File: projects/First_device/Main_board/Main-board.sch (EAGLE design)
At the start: 52 parts, among them Q1 BC847ALT1SMD, Q2 BC847ALT1SMD, Q3 BC847ALT1SMD, Q4 BC847ALT1SMD, T1 BCR108E6327, T2 BCR108E6327, T3 BCR108E6327, T4 BCR108E6327, X1 2EHDCR-5.08-10P, X2 2EHDCR-5.08-08P

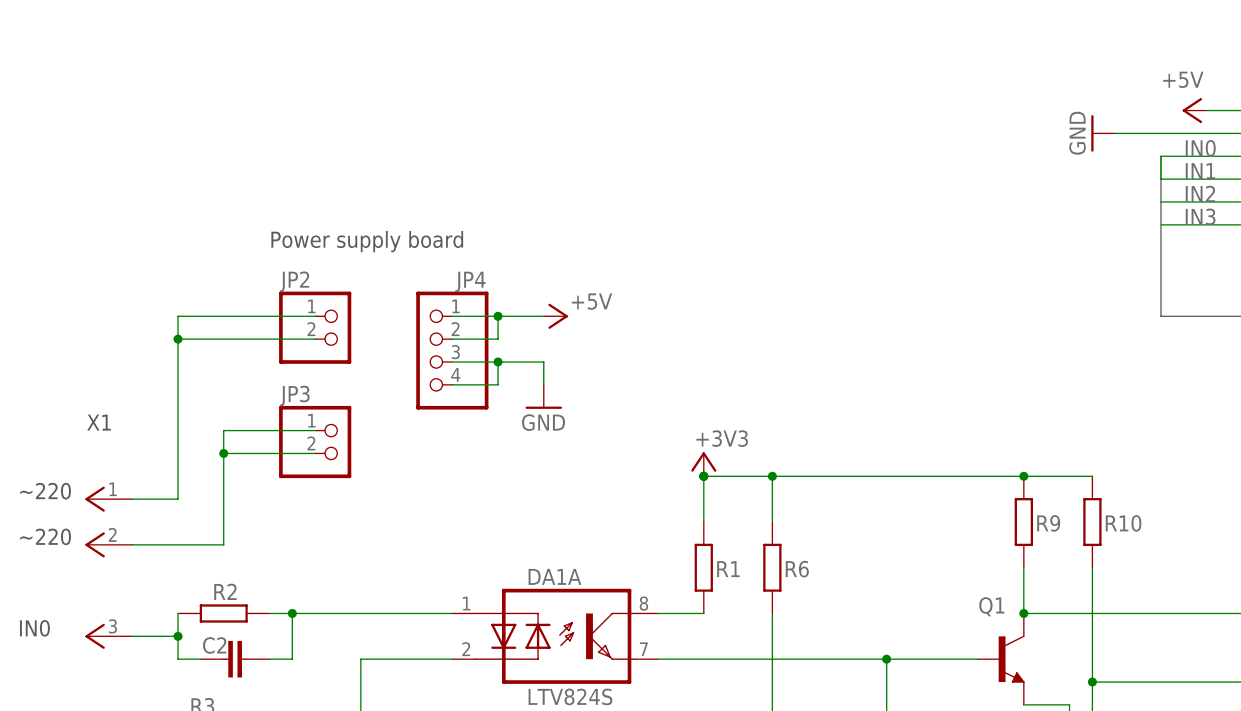
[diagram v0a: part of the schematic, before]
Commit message: AC/DC converter is added
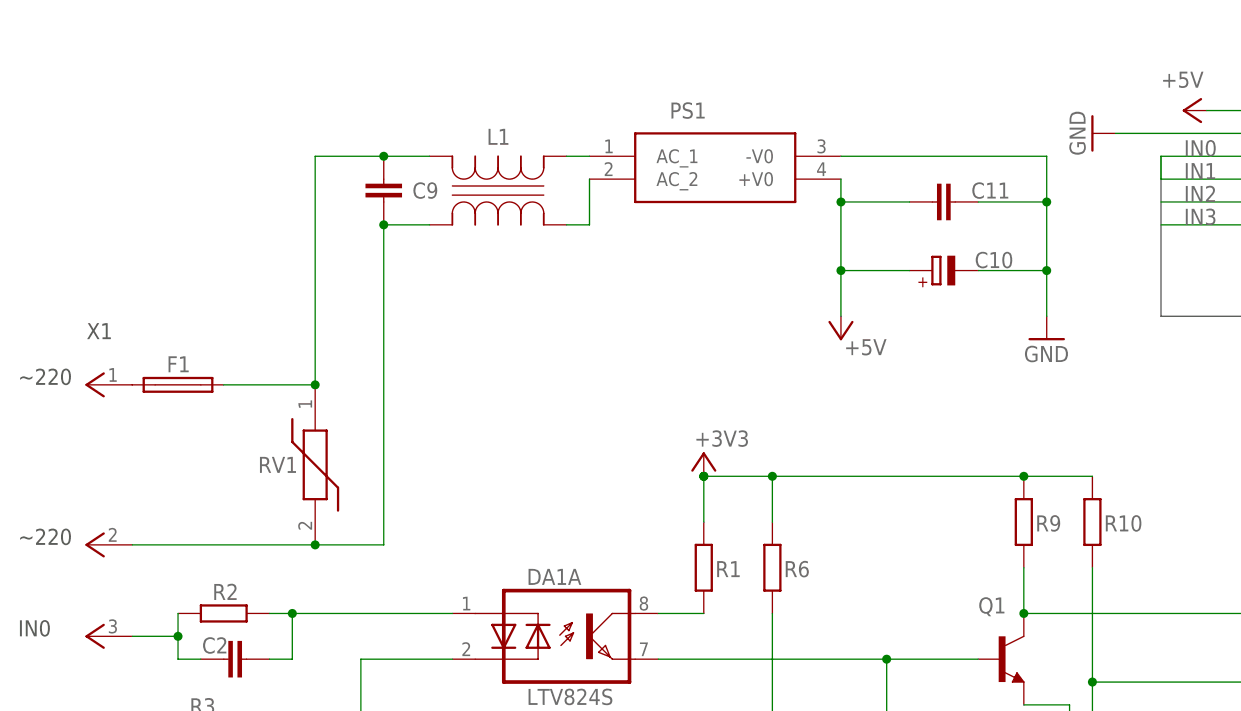
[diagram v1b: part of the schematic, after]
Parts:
- removed JP2, JP3: NOT INSTALLED, pinhead:PINHD-1X2
- removed JP4: NOT INSTALLED, pinhead:PINHD-1X4
- added C10: 220uF, rcl:CPOL-EUD/7343-31W
- added C11: 0,1u, rcl:C-EUC0603
- added C9: R46KI310000M1K, My_lib:R46KI310000M1K
- added F1: 0,5A, fuse:TR5
- added L1: DLW5BSN152SQ2L, My_lib:DLW5BSN152SQ2L
- added PS1: HLK-10M05, My_lib:HLK-10M05
- added RV1: VDR-10D561KJ, My_lib:VDR-10D561KJ
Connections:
- new net N$12: C9.2, F1.1, L1.1, RV1.1
- new net N$13: L1.2, PS1.AC_1
- new net N$26: C9.1, L1.4, RV1.2, X1G$2.1
- net +5V: now also C10.+, C11.1, PS1.+V0; no longer JP4.1, JP4.2
- net GND: now also C10.-, C11.2, PS1.-V0; no longer JP4.3, JP4.4
- net N$15: now also L1.3, PS1.AC_2; no longer JP3.1, JP3.2, X1G$2.1
- net N$16: now also F1.2; no longer JP2.1, JP2.2
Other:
- note removed: "Power supply board"

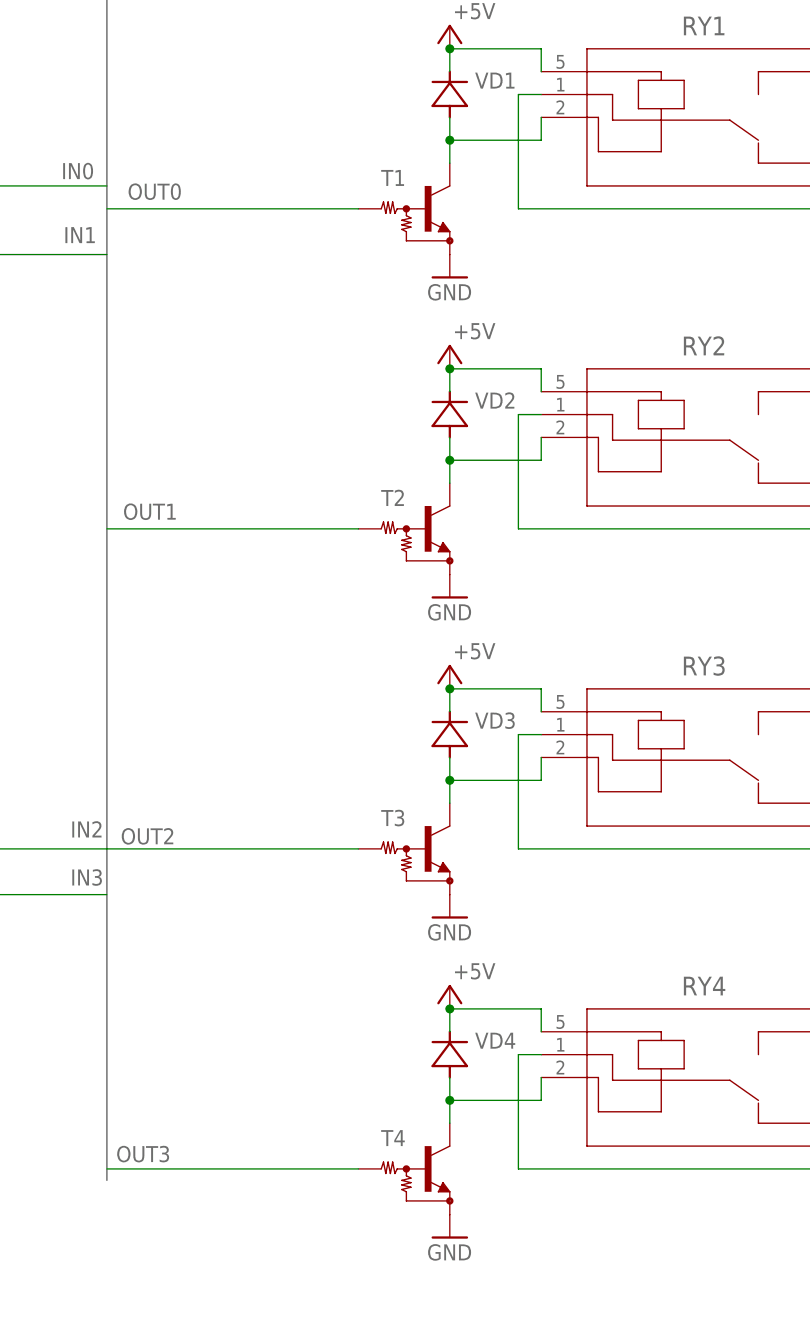
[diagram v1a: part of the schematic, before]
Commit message: Update BCR108 on main board
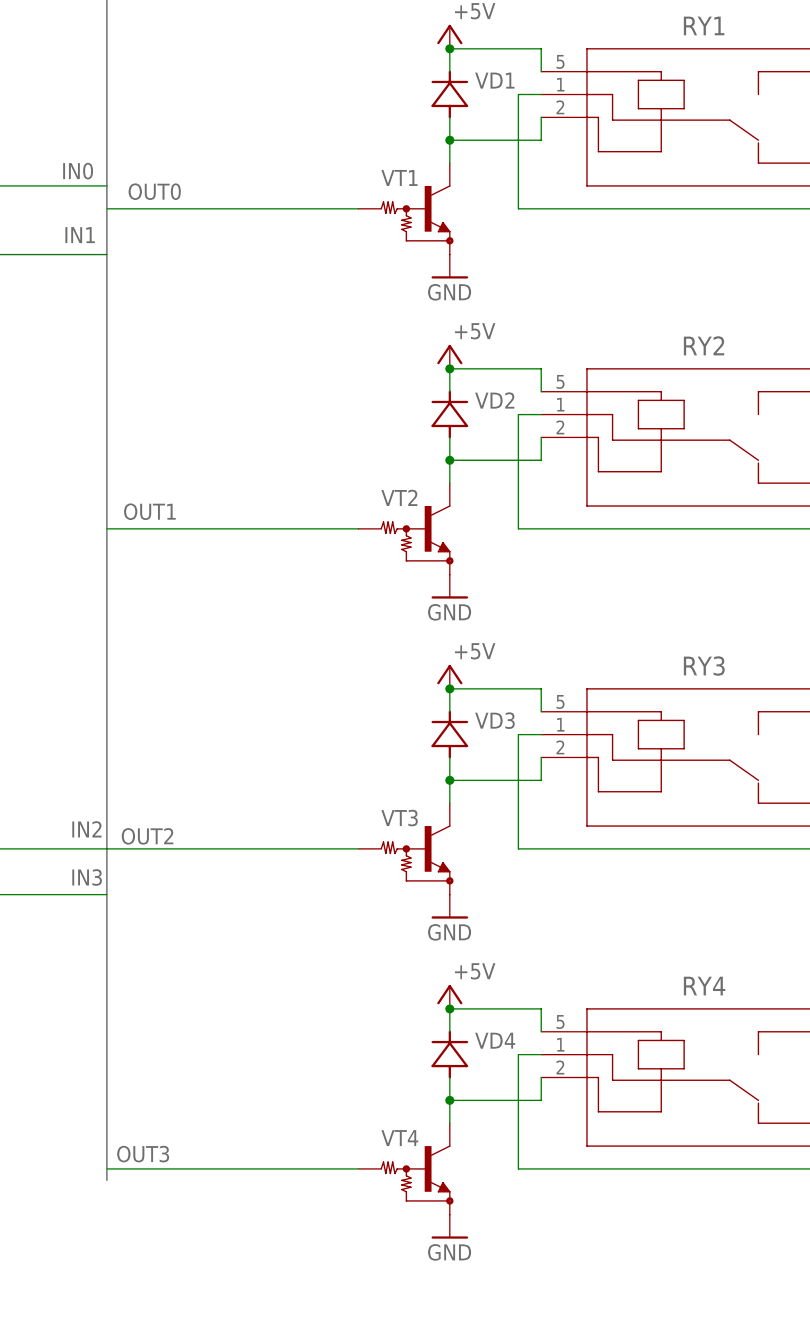
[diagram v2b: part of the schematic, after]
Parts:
- removed T1, T2, T3, T4: BCR108E6327, My_lib:BCR108BCR108E6327SC59-BEC
- added VT1, VT2, VT3, VT4: BCR108E6327, My_lib:BCR108E6327
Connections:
- net GND: now also VT1.2, VT2.2, VT3.2, VT4.2; no longer T1.E, T2.E, T3.E, T4.E
- net N$33: now also VT2.3; no longer T2.C
- net N$34: now also VT1.3; no longer T1.C
- net N$35: now also VT3.3; no longer T3.C
- net N$36: now also VT4.3; no longer T4.C
- net OUT0: now also VT1.1; no longer T1.B
- net OUT1: now also VT2.1; no longer T2.B
- net OUT2: now also VT3.1; no longer T3.B
- net OUT3: now also VT4.1; no longer T4.B
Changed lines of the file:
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@@
 </part>
 <part name="VD1" library="My_lib" deviceset="LL4148" device="" package3d_urn="urn:adsk.eagle:package:43405/2"/>
-<part name="T1" library="My_lib" deviceset="BCR108" device="SC59-BEC" package3d_urn="urn:adsk.eagle:package:28754/2" technology="BCR108E6327" value="BCR108E6327 "/>
 <part name="X1" library="My_lib" deviceset="2EHDCR-5.08-10P" device=""/>
 <part name="X2" library="My_lib" deviceset="2EHDCR-5.08-08P" device=""/>
@@
 <part name="P+1" library="supply1" library_urn="urn:adsk.eagle:library:371" deviceset="+5V" device=""/>
 <part name="VD2" library="My_lib" deviceset="LL4148" device="" package3d_urn="urn:adsk.eagle:package:43405/2"/>
-<part name="T2" library="My_lib" deviceset="BCR108" device="SC59-BEC" package3d_urn="urn:adsk.eagle:package:28754/2" technology="BCR108E6327" value="BCR108E6327 "/>
 <part name="GND4" library="supply1" library_urn="urn:adsk.eagle:library:371" deviceset="GND" device=""/>
 <part name="P+2" library="supply1" library_urn="urn:adsk.eagle:library:371" deviceset="+5V" device=""/>
 <part name="VD3" library="My_lib" deviceset="LL4148" device="" package3d_urn="urn:adsk.eagle:package:43405/2"/>
-<part name="T3" library="My_lib" deviceset="BCR108" device="SC59-BEC" package3d_urn="urn:adsk.eagle:package:28754/2" technology="BCR108E6327" value="BCR108E6327 "/>
 <part name="GND5" library="supply1" library_urn="urn:adsk.eagle:library:371" deviceset="GND" device=""/>
 <part name="P+3" library="supply1" library_urn="urn:adsk.eagle:library:371" deviceset="+5V" device=""/>
 <part name="VD4" library="My_lib" deviceset="LL4148" device="" package3d_urn="urn:adsk.eagle:package:43405/2"/>
-<part name="T4" library="My_lib" deviceset="BCR108" device="SC59-BEC" package3d_urn="urn:adsk.eagle:package:28754/2" technology="BCR108E6327" value="BCR108E6327 "/>
 <part name="GND6" library="supply1" library_urn="urn:adsk.eagle:library:371" deviceset="GND" device=""/>
 <part name="P+4" library="supply1" library_urn="urn:adsk.eagle:library:371" deviceset="+5V" device=""/>
@@
 <attribute name="VOLTAGE" value="50V"/>
 </part>
+<part name="VT1" library="My_lib" deviceset="BCR108" device="E6327"/>
+<part name="VT2" library="My_lib" deviceset="BCR108" device="E6327"/>
+<part name="VT3" library="My_lib" deviceset="BCR108" device="E6327"/>
+<part name="VT4" library="My_lib" deviceset="BCR108" device="E6327"/>
 </parts>
 <sheets>
@@
 <attribute name="NAME" x="129.3114" y="98.9584" size="1.778" layer="95" rot="R180"/>
 </instance>
-<instance part="T1" gate="G$1" x="119.38" y="83.82" smashed="yes">
-<attribute name="NAME" x="114.3" y="86.36" size="1.778" layer="95"/>
-<attribute name="VALUE" x="109.22" y="88.9" size="1.778" layer="96" display="off"/>
-</instance>
 <instance part="X1" gate="G$1" x="-53.34" y="106.68" smashed="yes"/>
 <instance part="X1" gate="G$2" x="-53.34" y="88.9" smashed="yes"/>
@@
 <attribute name="NAME" x="129.3114" y="63.3984" size="1.778" layer="95" rot="R180"/>
 </instance>
-<instance part="T2" gate="G$1" x="119.38" y="48.26" smashed="yes">
-<attribute name="NAME" x="114.3" y="50.8" size="1.778" layer="95"/>
-<attribute name="VALUE" x="109.22" y="53.34" size="1.778" layer="96" display="off"/>
-</instance>
 <instance part="GND4" gate="1" x="121.92" y="40.64" smashed="yes">
 <attribute name="VALUE" x="119.38" y="38.1" size="1.778" layer="96"/>
@@
 <attribute name="NAME" x="129.3114" y="27.8384" size="1.778" layer="95" rot="R180"/>
 </instance>
-<instance part="T3" gate="G$1" x="119.38" y="12.7" smashed="yes">
-<attribute name="NAME" x="114.3" y="15.24" size="1.778" layer="95"/>
-<attribute name="VALUE" x="109.22" y="17.78" size="1.778" layer="96" display="off"/>
-</instance>
 <instance part="GND5" gate="1" x="121.92" y="5.08" smashed="yes">
 <attribute name="VALUE" x="119.38" y="2.54" size="1.778" layer="96"/>
@@
 <instance part="VD4" gate="G$1" x="121.92" y="-10.16" smashed="yes" rot="R90">
 <attribute name="NAME" x="129.3114" y="-7.7216" size="1.778" layer="95" rot="R180"/>
-</instance>
-<instance part="T4" gate="G$1" x="119.38" y="-22.86" smashed="yes">
-<attribute name="NAME" x="114.3" y="-20.32" size="1.778" layer="95"/>
-<attribute name="VALUE" x="109.22" y="-17.78" size="1.778" layer="96" display="off"/>
 </instance>
 <instance part="GND6" gate="1" x="121.92" y="-30.48" smashed="yes">
@@
 <attribute name="STYPE" x="38.1" y="132.08" size="1.778" layer="96" rot="R90" display="off"/>
 <attribute name="VOLTAGE" x="38.1" y="132.08" size="1.778" layer="96" rot="R90" display="off"/>
+</instance>
+<instance part="VT1" gate="G$1" x="119.38" y="83.82" smashed="yes">
+<attribute name="NAME" x="114.3" y="86.36" size="1.778" layer="95"/>
+<attribute name="VALUE" x="109.22" y="88.9" size="1.778" layer="96" display="off"/>
+</instance>
+<instance part="VT2" gate="G$1" x="119.38" y="48.26" smashed="yes">
+<attribute name="NAME" x="114.3" y="50.8" size="1.778" layer="95"/>
+<attribute name="VALUE" x="109.22" y="53.34" size="1.778" layer="96" display="off"/>
+</instance>
+<instance part="VT3" gate="G$1" x="119.38" y="12.7" smashed="yes">
+<attribute name="NAME" x="114.3" y="15.24" size="1.778" layer="95"/>
+<attribute name="VALUE" x="109.22" y="17.78" size="1.778" layer="96" display="off"/>
+</instance>
+<instance part="VT4" gate="G$1" x="119.38" y="-22.86" smashed="yes">
+<attribute name="NAME" x="114.3" y="-20.32" size="1.778" layer="95"/>
+<attribute name="VALUE" x="109.22" y="-17.78" size="1.778" layer="96" display="off"/>
 </instance>
 </instances>
@@
 </segment>
 <segment>
-<pinref part="GND3" gate="1" pin="GND"/>
-<pinref part="T1" gate="G$1" pin="E"/>
-</segment>
-<segment>
-<pinref part="GND4" gate="1" pin="GND"/>
-<pinref part="T2" gate="G$1" pin="E"/>
-</segment>
-<segment>
-<pinref part="GND5" gate="1" pin="GND"/>
-<pinref part="T3" gate="G$1" pin="E"/>
-</segment>
-<segment>
-<pinref part="GND6" gate="1" pin="GND"/>
-<pinref part="T4" gate="G$1" pin="E"/>
-</segment>
-<segment>
 <pinref part="GND7" gate="1" pin="GND"/>
 <wire x1="58.42" y1="139.7" x2="78.74" y2="139.7" width="0.1524" layer="91"/>
@@
 <wire x1="43.18" y1="124.46" x2="50.8" y2="124.46" width="0.1524" layer="91"/>
 <junction x="50.8" y="124.46"/>
+</segment>
+<segment>
+<pinref part="GND3" gate="1" pin="GND"/>
+<pinref part="VT1" gate="G$1" pin="2"/>
+</segment>
+<segment>
+<pinref part="VT2" gate="G$1" pin="2"/>
+<pinref part="GND4" gate="1" pin="GND"/>
+</segment>
+<segment>
+<pinref part="VT3" gate="G$1" pin="2"/>
+<pinref part="GND5" gate="1" pin="GND"/>
+</segment>
+<segment>
+<pinref part="VT4" gate="G$1" pin="2"/>
+<pinref part="GND6" gate="1" pin="GND"/>
 </segment>
 </net>
@@
 <wire x1="121.92" y1="88.9" x2="121.92" y2="91.44" width="0.1524" layer="91"/>
 <junction x="121.92" y="91.44"/>
-<pinref part="T1" gate="G$1" pin="C"/>
+<pinref part="VT1" gate="G$1" pin="3"/>
 </segment>
 </net>
@@
 <wire x1="121.92" y1="53.34" x2="121.92" y2="55.88" width="0.1524" layer="91"/>
 <junction x="121.92" y="55.88"/>
-<pinref part="T2" gate="G$1" pin="C"/>
 <pinref part="RY2" gate="A" pin="2"/>
 <wire x1="132.08" y1="58.42" x2="132.08" y2="55.88" width="0.1524" layer="91"/>
+<pinref part="VT2" gate="G$1" pin="3"/>
 </segment>
 </net>
@@
 <wire x1="121.92" y1="17.78" x2="121.92" y2="20.32" width="0.1524" layer="91"/>
 <junction x="121.92" y="20.32"/>
-<pinref part="T3" gate="G$1" pin="C"/>
 <pinref part="RY3" gate="A" pin="2"/>
 <wire x1="132.08" y1="22.86" x2="132.08" y2="20.32" width="0.1524" layer="91"/>
+<pinref part="VT3" gate="G$1" pin="3"/>
 </segment>
 </net>
@@
 <wire x1="121.92" y1="-17.78" x2="121.92" y2="-15.24" width="0.1524" layer="91"/>
 <junction x="121.92" y="-15.24"/>
-<pinref part="T4" gate="G$1" pin="C"/>
 <pinref part="RY4" gate="A" pin="2"/>
 <wire x1="132.08" y1="-12.7" x2="132.08" y2="-15.24" width="0.1524" layer="91"/>
+<pinref part="VT4" gate="G$1" pin="3"/>
 </segment>
 </net>
@@
 <net name="OUT0" class="0">
 <segment>
-<pinref part="T1" gate="G$1" pin="B"/>
 <wire x1="83.82" y1="83.82" x2="111.76" y2="83.82" width="0.1524" layer="91"/>
 <label x="86.106" y="84.836" size="1.778" layer="95"/>
+<pinref part="VT1" gate="G$1" pin="1"/>
 </segment>
 <segment>
@@
 <net name="OUT1" class="0">
 <segment>
-<pinref part="T2" gate="G$1" pin="B"/>
 <wire x1="83.82" y1="48.26" x2="111.76" y2="48.26" width="0.1524" layer="91"/>
 <label x="85.598" y="49.276" size="1.778" layer="95"/>
+<pinref part="VT2" gate="G$1" pin="1"/>
 </segment>
 <segment>
@@
 <net name="OUT2" class="0">
 <segment>
-<pinref part="T3" gate="G$1" pin="B"/>
 <wire x1="83.82" y1="12.7" x2="111.76" y2="12.7" width="0.1524" layer="91"/>
 <label x="85.344" y="13.208" size="1.778" layer="95"/>
+<pinref part="VT3" gate="G$1" pin="1"/>
 </segment>
 <segment>
@@
 <net name="OUT3" class="0">
 <segment>
-<pinref part="T4" gate="G$1" pin="B"/>
 <wire x1="83.82" y1="-22.86" x2="111.76" y2="-22.86" width="0.1524" layer="91"/>
 <label x="84.836" y="-22.098" size="1.778" layer="95"/>
-</segment>
-<segment>
+<pinref part="VT4" gate="G$1" pin="1"/>
+</segment>
+<segment>
